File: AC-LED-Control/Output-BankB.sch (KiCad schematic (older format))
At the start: 58 parts, among them P201 CONN_01X02, P202 CONN_01X02, P203 CONN_01X02, P204 CONN_01X02, P205 CONN_01X02, P206 CONN_01X02, P207 CONN_01X02, P208 CONN_01X02, U201 LTV-846S, U202 LTV-846S, U203 TRIAC, U204 TRIAC, U205 TRIAC, U206 TRIAC, U207 TRIAC, U208 TRIAC, U209 TRIAC, U210 TRIAC

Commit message: more stuff
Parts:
- renumbered 22nF203 to 22nF202, 22nF205 to 22nF203, 22nF207 to 22nF204, 22nF202 to 22nF205, 22nF204 to 22nF206, 22nF206 to 22nF207, P203 to P202, P205 to P203, P207 to P204, P202 to P205, P204 to P206, P206 to P207, R207 to R202, R211 to R203, R213 to R204, R209 to R205, R219 to R206, R225 to R207, R231 to R208, R202 to R209, R215 to R210, R221 to R211, R227 to R212, R203 to R213, R216 to R214, R222 to R215, R228 to R216, R204 to R217, R208 to R218, R212 to R219, R214 to R220, R210 to R221, R220 to R222, R226 to R223, R232 to R224, R205 to R225, R217 to R226, R223 to R227, R229 to R228, R206 to R229, R218 to R230, R224 to R231, R230 to R232, U203 to U202, U205 to U203, U207 to U204, U209 to U205, U202 to U206, U204 to U207, U206 to U208, U208 to U209

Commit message: Associated footprints
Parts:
- C201: renamed from 22nF201; value C -> 22nF; footprint (none) -> Capacitors_SMD:C_0603_HandSoldering
- C202: renamed from 22nF202; value C -> 22nF; footprint (none) -> Capacitors_SMD:C_0603_HandSoldering
- C203: renamed from 22nF203; value C -> 22nF; footprint (none) -> Capacitors_SMD:C_0603_HandSoldering
- C204: renamed from 22nF204; value C -> 22nF; footprint (none) -> Capacitors_SMD:C_0603_HandSoldering
- C205: renamed from 22nF205; value C -> 22nF; footprint (none) -> Capacitors_SMD:C_0603_HandSoldering
- C206: renamed from 22nF206; value C -> 22nF; footprint (none) -> Capacitors_SMD:C_0603_HandSoldering
- C207: renamed from 22nF207; value C -> 22nF; footprint (none) -> Capacitors_SMD:C_0603_HandSoldering
- C208: renamed from 22nF208; value C -> 22nF; footprint (none) -> Capacitors_SMD:C_0603_HandSoldering
- P201, P202, P203, P204, P205, P206, P207, P208: footprint (none) -> Pin_Headers:Pin_Header_Straight_1x02
- R201, R202, R203, R204, R205, R206, R207, R208, R209, R210, R211, R212, R213, R214, R215, R216, R217, R218, R219, R220, R221, R222, R223, R224, R225, R226, R227, R228, R229, R230, R231, R232: footprint (none) -> Resistors_SMD:R_0603_HandSoldering
- U201, U206: footprint (none) -> lite-on:Lite-On_SMD-16

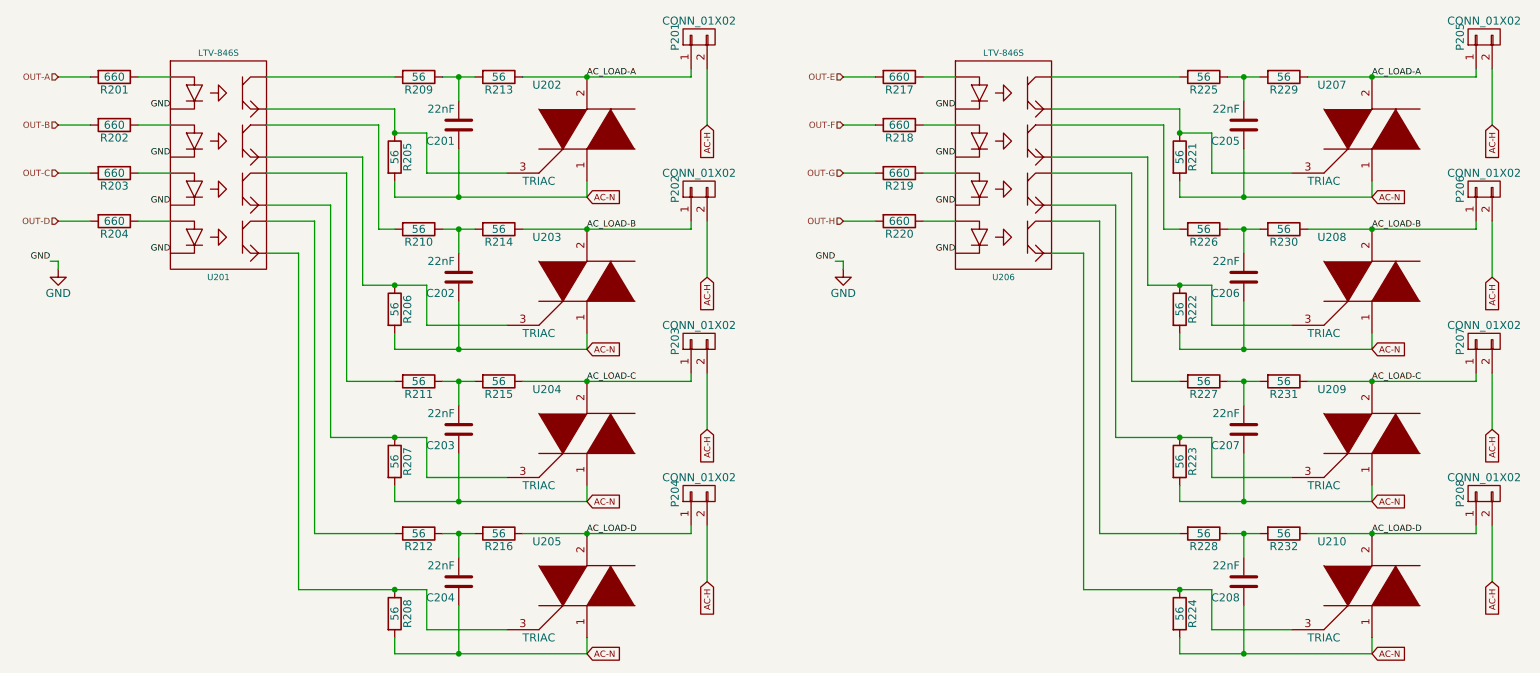
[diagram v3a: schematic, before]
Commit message: Added 3v3 power regulator
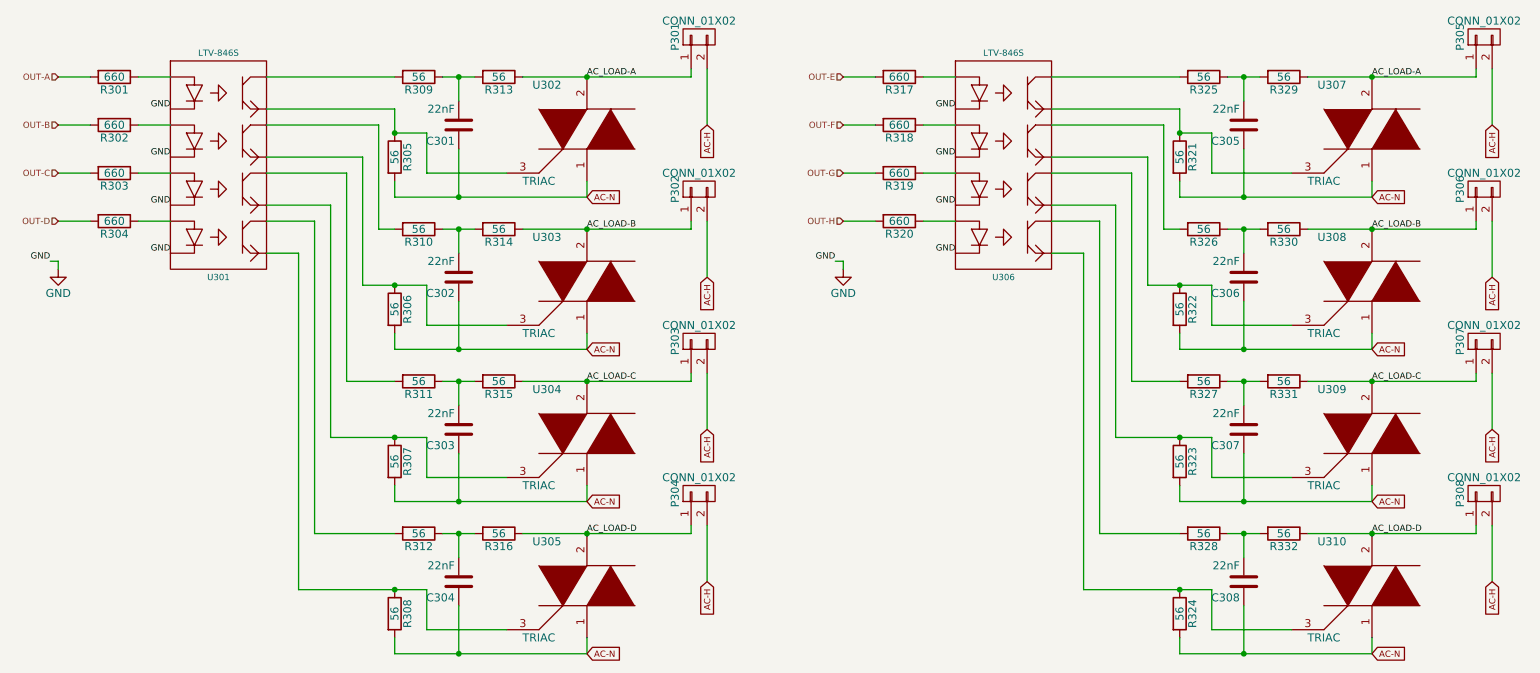
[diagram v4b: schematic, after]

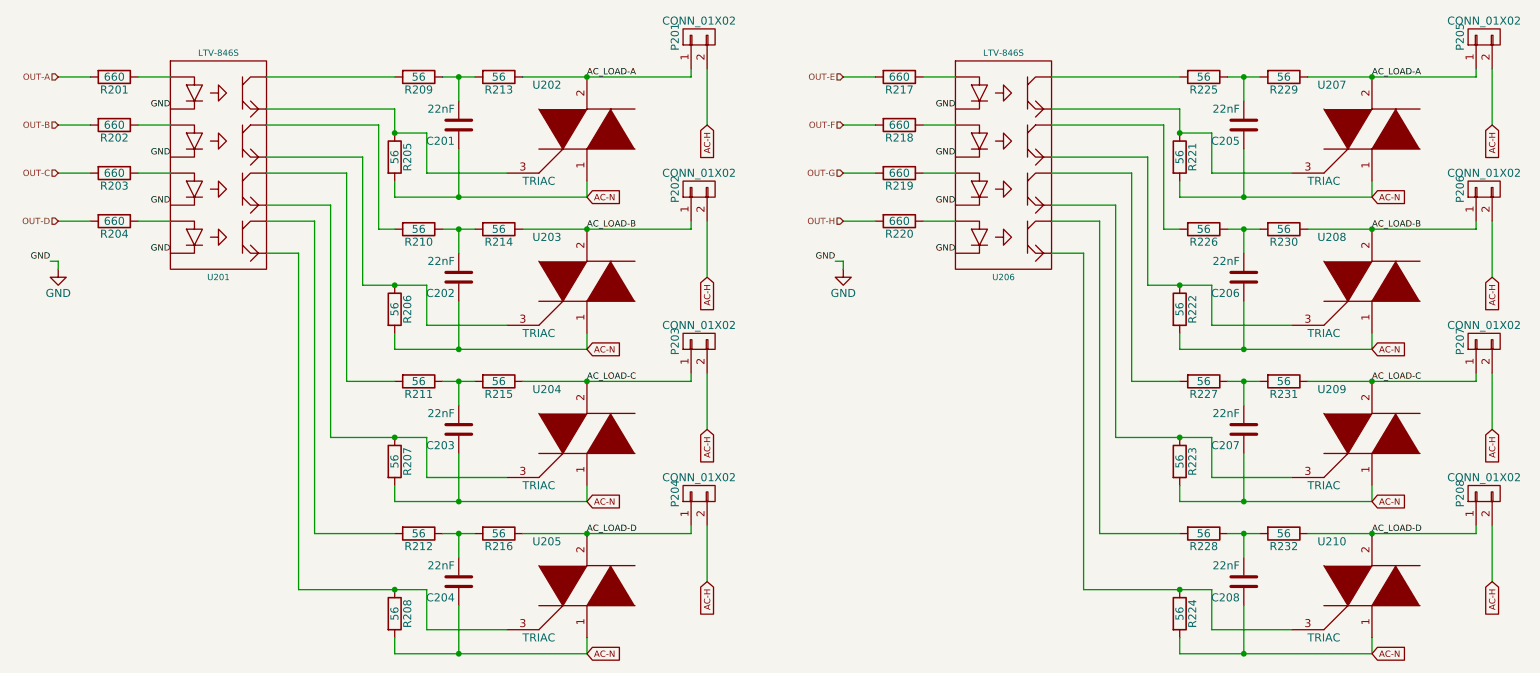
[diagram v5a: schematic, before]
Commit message: Changed up isolation scheme and added BOM
Instead of isolating each of the TRIAC channels individually,
I changed it so the system uses an isolated power supply and isolates
itself from I2C as well.

Basic BOM was started as well.
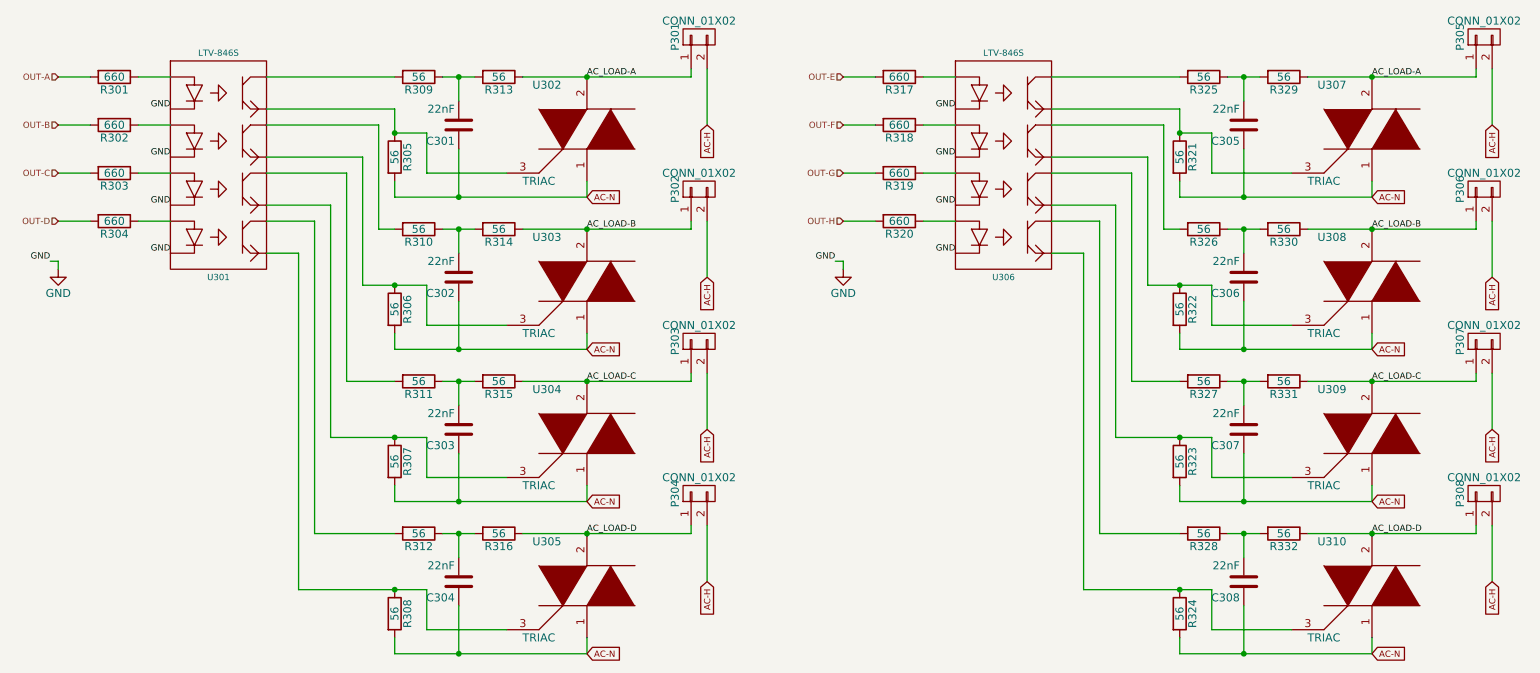
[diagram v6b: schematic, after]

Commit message: Modified some values for finding components
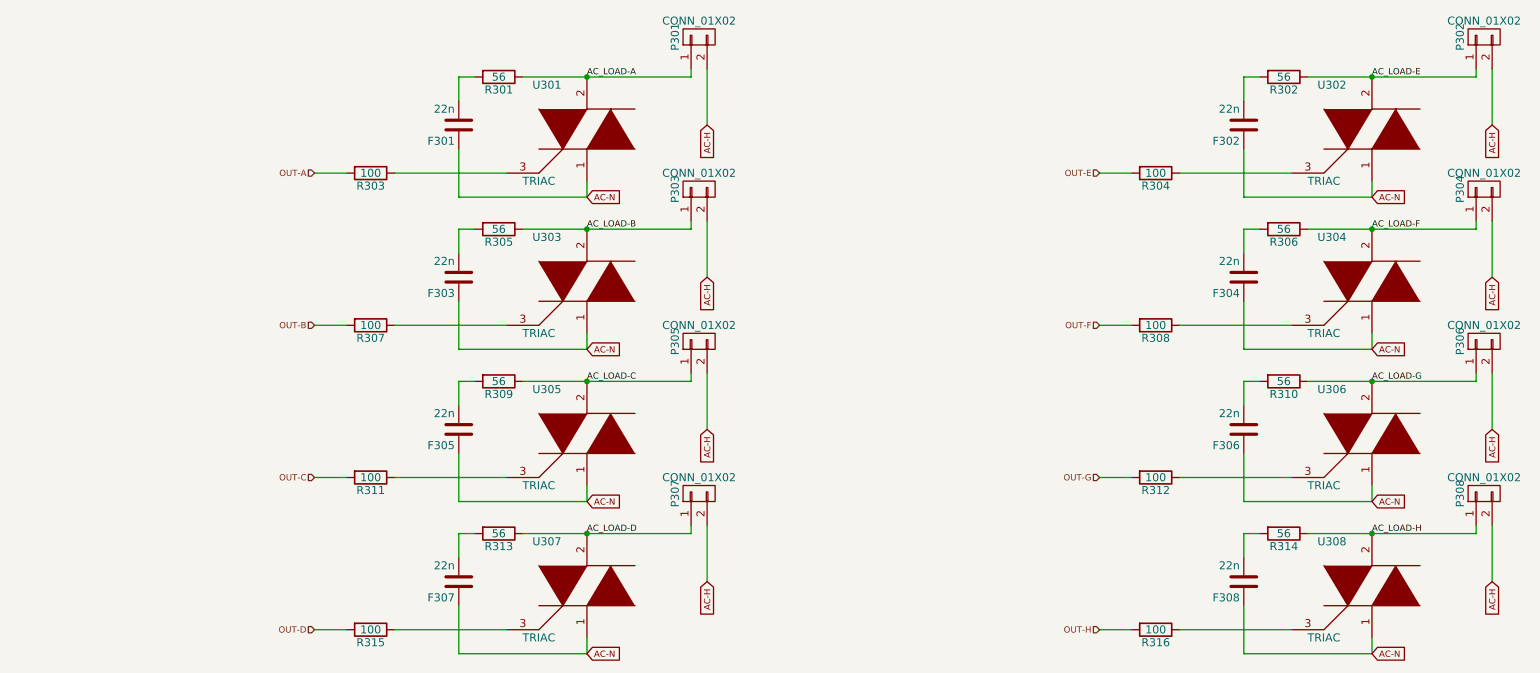
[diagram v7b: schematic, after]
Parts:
- removed R205, R206, R207, R208, R209, R210, R211, R212, R221, R222, R223, R224, R225, R226, R227, R228: 56, Resistors_SMD:R_0603_HandSoldering, symbol R
- removed U201, U206: LTV-846S, lite-on:Lite-On_SMD-16, symbol LTV-846S
- F201: renamed from C201; value 22nF -> 22n
- F202: renamed from C205; value 22nF -> 22n
- F203: renamed from C202; value 22nF -> 22n
- F204: renamed from C206; value 22nF -> 22n
- F205: renamed from C203; value 22nF -> 22n
- F206: renamed from C207; value 22nF -> 22n
- F207: renamed from C204; value 22nF -> 22n
- F208: renamed from C208; value 22nF -> 22n
- P201, P208: footprint Pin_Headers:Pin_Header_Straight_1x02 -> Pin_Headers:Pin_Header_Straight_1x02_Pitch2.54mm
- P202: renamed from P205; footprint Pin_Headers:Pin_Header_Straight_1x02 -> Pin_Headers:Pin_Header_Straight_1x02_Pitch2.54mm
- P203: renamed from P202; footprint Pin_Headers:Pin_Header_Straight_1x02 -> Pin_Headers:Pin_Header_Straight_1x02_Pitch2.54mm
- P204: renamed from P206; footprint Pin_Headers:Pin_Header_Straight_1x02 -> Pin_Headers:Pin_Header_Straight_1x02_Pitch2.54mm
- P205: renamed from P203; footprint Pin_Headers:Pin_Header_Straight_1x02 -> Pin_Headers:Pin_Header_Straight_1x02_Pitch2.54mm
- P206: renamed from P207; footprint Pin_Headers:Pin_Header_Straight_1x02 -> Pin_Headers:Pin_Header_Straight_1x02_Pitch2.54mm
- P207: renamed from P204; footprint Pin_Headers:Pin_Header_Straight_1x02 -> Pin_Headers:Pin_Header_Straight_1x02_Pitch2.54mm
- R203: renamed from R201; value 660 -> 100
- R204: renamed from R217; value 660 -> 100
- R207: renamed from R202; value 660 -> 100
- R208: renamed from R218; value 660 -> 100
- R211: renamed from R203; value 660 -> 100
- R212: renamed from R219; value 660 -> 100
- R215: renamed from R204; value 660 -> 100
- R216: renamed from R220; value 660 -> 100
- renumbered R213 to R201, R229 to R202, R214 to R205, R230 to R206, R215 to R209, R231 to R210, R216 to R213, R232 to R214, U202 to U201, U207 to U202, U208 to U204, U204 to U205, U209 to U206, U205 to U207, U210 to U208
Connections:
- net AC_LOAD-A: no longer P202.1 (P1), R202.1, U202.2
- net AC_LOAD-B: no longer P204.1 (P1), R206.1, U204.2
- net AC_LOAD-C: no longer P206.1 (P1), R210.1, U206.2
- net AC_LOAD-D: no longer P208.1 (P1), R214.1, U208.2
- net at R203.1: now also U201.3
- net at U205.3: now also R211.1
- net at U203.3: now also R207.1
- net at R215.1: now also U207.3
- net at R204.1: now also U202.3
- net at U206.3: now also R212.1
- net at U204.3: now also R208.1
- net at R216.1: now also U208.3
- new net AC_LOAD-E: P202.1 (P1), R202.1, U202.2
- new net AC_LOAD-F: P204.1 (P1), R206.1, U204.2
- new net AC_LOAD-G: P206.1 (P1), R210.1, U206.2
- new net AC_LOAD-H: P208.1 (P1), R214.1, U208.2
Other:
- moved on the sheet: R303, R304, R307, R308, R311, R312, R315, R316
